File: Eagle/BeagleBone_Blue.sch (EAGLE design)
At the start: 153 parts, among them M1 JST_ZH_2, M2 JST_ZH_2, M3 JST_ZH_2, M4 JST_ZH_2, Q3 MOSFET-N, U1 OSD3358, U2 CM200C-32.768KAZF-UT, U3 DMC564040R, U4 DMC564040R, U5 24LC_32AT-I/OT

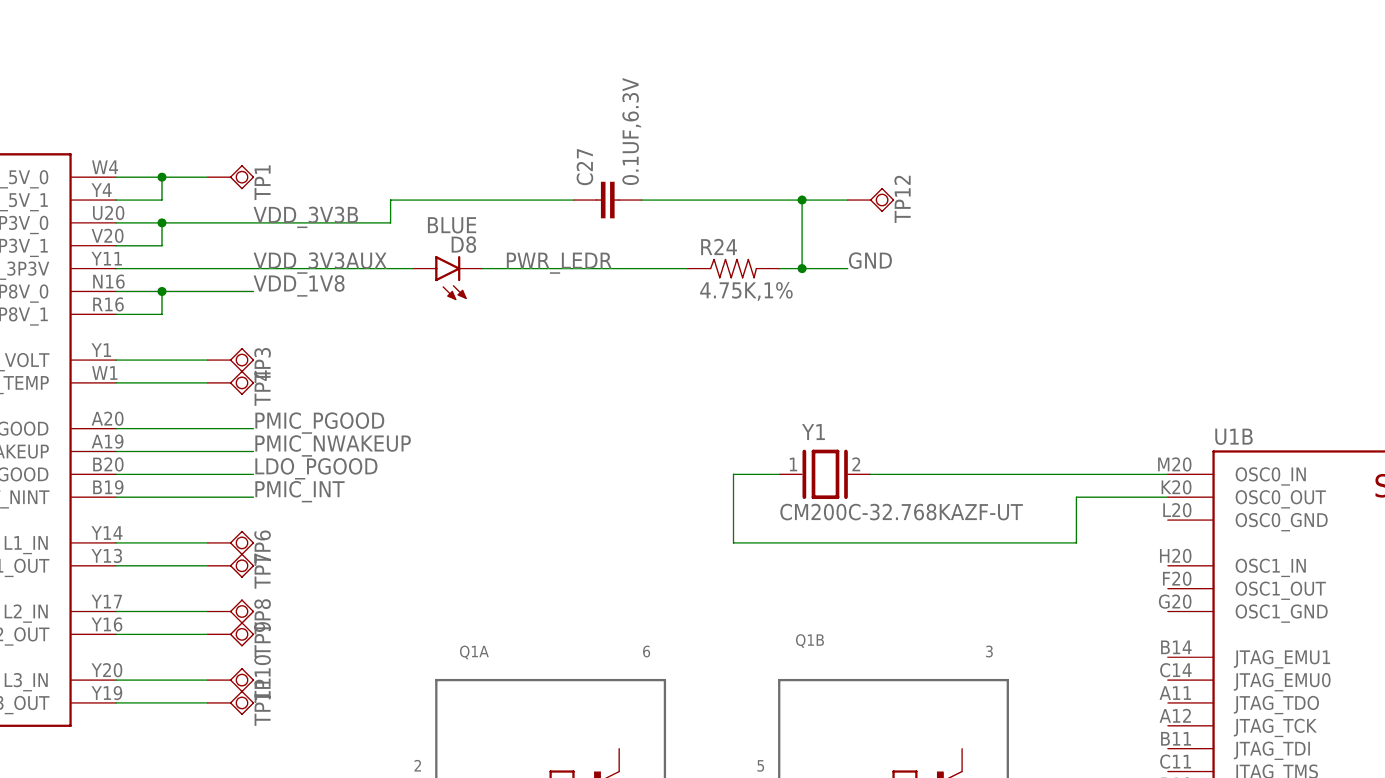
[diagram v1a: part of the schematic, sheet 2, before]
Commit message: Added crystals
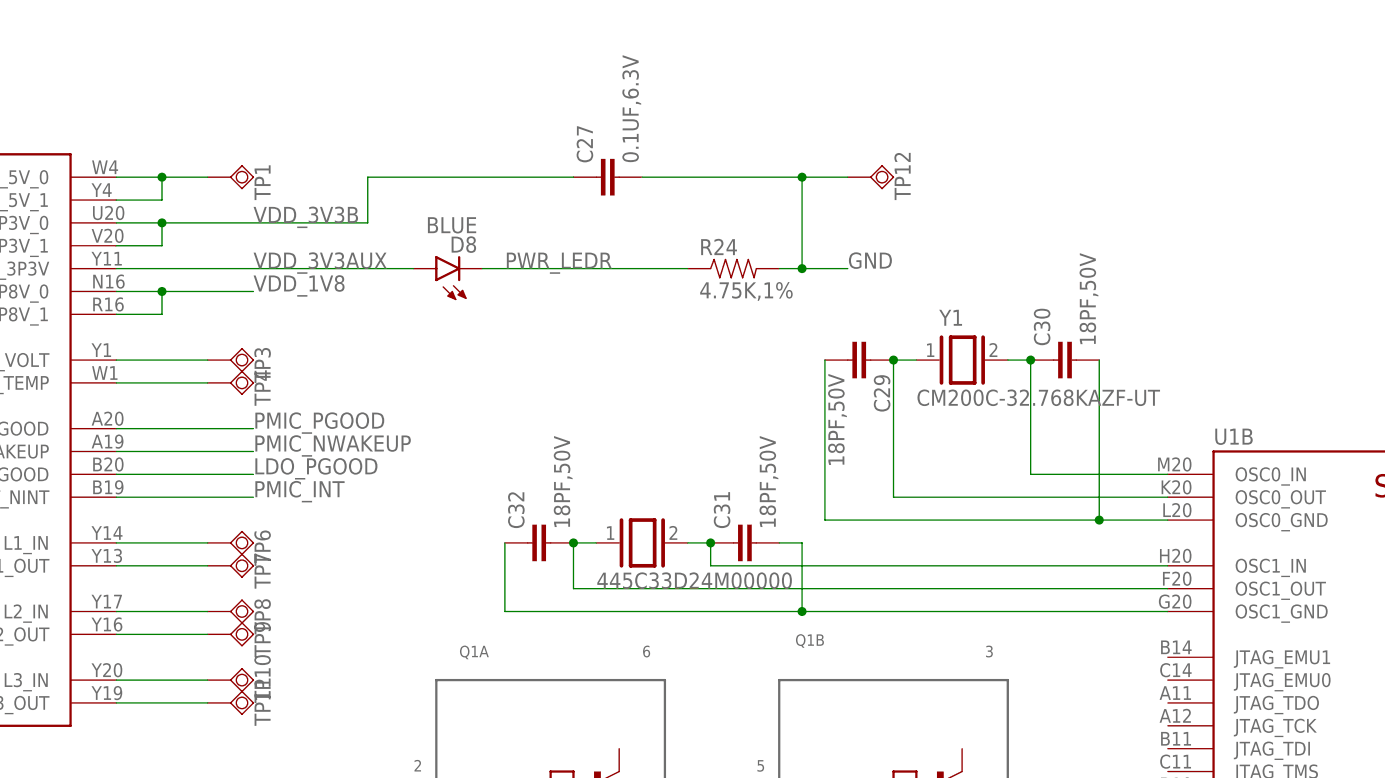
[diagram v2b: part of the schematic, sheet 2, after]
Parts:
- added C29, C30, C31, C32: 18PF,50V, Strawson_Eagle_Lib:CAP0402-CAP
- added Y2: 445C33D24M00000, 445C33D24M00000:445C33D24M00000
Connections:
- new net N$31: C29.2, C30.2, U1B.OSC0_GND
- new net N$32: C31.1, U1B.OSC1_IN, Y2.2
- new net N$33: C32.2, U1B.OSC1_OUT, Y2.1
- new net N$34: C31.2, C32.1, U1B.OSC1_GND
- net N$26: now also C30.1
- net N$27: now also C29.1
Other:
- moved on the sheet: C27, TP12
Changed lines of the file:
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@@
 <part name="TP13" library="testpad" deviceset="TPSQ" device="B1,27"/>
 <part name="C28" library="Strawson_Eagle_Lib" deviceset="CAP" device="0402-CAP" value="0.1UF,6.3V"/>
+<part name="C29" library="Strawson_Eagle_Lib" deviceset="CAP" device="0402-CAP" value="18PF,50V"/>
+<part name="C30" library="Strawson_Eagle_Lib" deviceset="CAP" device="0402-CAP" value="18PF,50V"/>
+<part name="Y2" library="445C33D24M00000" deviceset="445C33D24M00000" device=""/>
+<part name="C31" library="Strawson_Eagle_Lib" deviceset="CAP" device="0402-CAP" value="18PF,50V"/>
+<part name="C32" library="Strawson_Eagle_Lib" deviceset="CAP" device="0402-CAP" value="18PF,50V"/>
 </parts>
 <sheets>
@@
 <instance part="TP10" gate="G$1" x="137.16" y="193.04" rot="R90"/>
 <instance part="TP11" gate="G$1" x="137.16" y="190.5" rot="R90"/>
-<instance part="TP12" gate="G$1" x="208.28" y="246.38" rot="R90"/>
-<instance part="C27" gate="G$1" x="180.34" y="246.38" rot="R90"/>
-<instance part="U2" gate="G$1" x="251.46" y="203.2"/>
+<instance part="TP12" gate="G$1" x="208.28" y="248.92" rot="R90"/>
+<instance part="C27" gate="G$1" x="180.34" y="248.92" rot="R90"/>
+<instance part="U2" gate="G$1" x="266.7" y="215.9"/>
 <instance part="U3" gate="G$1" x="195.58" y="175.26"/>
 <instance part="U4" gate="G$1" x="195.58" y="134.62"/>
@@
 <instance part="TP13" gate="G$1" x="48.26" y="157.48" rot="R270"/>
 <instance part="C28" gate="G$1" x="25.4" y="160.02"/>
+<instance part="C29" gate="G$1" x="205.74" y="228.6" rot="R270"/>
+<instance part="C30" gate="G$1" x="231.14" y="228.6" rot="R90"/>
+<instance part="Y2" gate="G$1" x="226.06" y="198.12"/>
+<instance part="C31" gate="G$1" x="195.58" y="208.28" rot="R90"/>
+<instance part="C32" gate="G$1" x="172.72" y="208.28" rot="R90"/>
 </instances>
 <busses>
@@
 <junction x="129.54" y="243.84"/>
 <label x="139.7" y="243.84" size="1.778" layer="95"/>
-<wire x1="129.54" y1="243.84" x2="154.94" y2="243.84" width="0.1524" layer="91"/>
-<wire x1="154.94" y1="243.84" x2="154.94" y2="246.38" width="0.1524" layer="91"/>
+<wire x1="129.54" y1="243.84" x2="152.4" y2="243.84" width="0.1524" layer="91"/>
+<wire x1="152.4" y1="243.84" x2="152.4" y2="248.92" width="0.1524" layer="91"/>
 <pinref part="C27" gate="G$1" pin="1"/>
-<wire x1="154.94" y1="246.38" x2="175.26" y2="246.38" width="0.1524" layer="91"/>
+<wire x1="152.4" y1="248.92" x2="175.26" y2="248.92" width="0.1524" layer="91"/>
 </segment>
 </net>
@@
 <pinref part="TP12" gate="G$1" pin="TP"/>
 <pinref part="C27" gate="G$1" pin="2"/>
-<wire x1="182.88" y1="246.38" x2="200.66" y2="246.38" width="0.1524" layer="91"/>
-<wire x1="200.66" y1="246.38" x2="205.74" y2="246.38" width="0.1524" layer="91"/>
+<wire x1="182.88" y1="248.92" x2="200.66" y2="248.92" width="0.1524" layer="91"/>
+<wire x1="200.66" y1="248.92" x2="205.74" y2="248.92" width="0.1524" layer="91"/>
 <wire x1="205.74" y1="238.76" x2="200.66" y2="238.76" width="0.1524" layer="91"/>
-<wire x1="200.66" y1="238.76" x2="200.66" y2="246.38" width="0.1524" layer="91"/>
-<junction x="200.66" y="246.38"/>
+<wire x1="200.66" y1="238.76" x2="200.66" y2="248.92" width="0.1524" layer="91"/>
+<junction x="200.66" y="248.92"/>
 <junction x="200.66" y="238.76"/>
 </segment>
@@
 <net name="N$26" class="0">
 <segment>
+<pinref part="U2" gate="G$1" pin="2"/>
+<pinref part="C30" gate="G$1" pin="1"/>
+<wire x1="226.06" y1="228.6" x2="223.52" y2="228.6" width="0.1524" layer="91"/>
+<wire x1="226.06" y1="228.6" x2="226.06" y2="215.9" width="0.1524" layer="91"/>
+<junction x="226.06" y="228.6"/>
 <pinref part="U1" gate="B" pin="OSC0_IN"/>
-<pinref part="U2" gate="G$1" pin="2"/>
-<wire x1="241.3" y1="215.9" x2="208.28" y2="215.9" width="0.1524" layer="91"/>
+<wire x1="226.06" y1="215.9" x2="241.3" y2="215.9" width="0.1524" layer="91"/>
 </segment>
 </net>
@@
 <segment>
 <pinref part="U1" gate="B" pin="OSC0_OUT"/>
-<wire x1="241.3" y1="213.36" x2="231.14" y2="213.36" width="0.1524" layer="91"/>
-<wire x1="231.14" y1="213.36" x2="231.14" y2="208.28" width="0.1524" layer="91"/>
-<wire x1="231.14" y1="208.28" x2="193.04" y2="208.28" width="0.1524" layer="91"/>
-<wire x1="193.04" y1="208.28" x2="193.04" y2="215.9" width="0.1524" layer="91"/>
+<wire x1="241.3" y1="213.36" x2="210.82" y2="213.36" width="0.1524" layer="91"/>
+<wire x1="210.82" y1="213.36" x2="210.82" y2="228.6" width="0.1524" layer="91"/>
 <pinref part="U2" gate="G$1" pin="1"/>
-<wire x1="193.04" y1="215.9" x2="198.12" y2="215.9" width="0.1524" layer="91"/>
+<wire x1="210.82" y1="228.6" x2="213.36" y2="228.6" width="0.1524" layer="91"/>
+<pinref part="C29" gate="G$1" pin="1"/>
+<junction x="210.82" y="228.6"/>
 </segment>
 </net>
@@
 </segment>
 </net>
+<net name="N$31" class="0">
+<segment>
+<pinref part="U1" gate="B" pin="OSC0_GND"/>
+<wire x1="241.3" y1="210.82" x2="233.68" y2="210.82" width="0.1524" layer="91"/>
+<pinref part="C29" gate="G$1" pin="2"/>
+<wire x1="233.68" y1="210.82" x2="203.2" y2="210.82" width="0.1524" layer="91"/>
+<wire x1="203.2" y1="210.82" x2="203.2" y2="228.6" width="0.1524" layer="91"/>
+<pinref part="C30" gate="G$1" pin="2"/>
+<wire x1="233.68" y1="228.6" x2="233.68" y2="210.82" width="0.1524" layer="91"/>
+<junction x="233.68" y="210.82"/>
+</segment>
+</net>
+<net name="N$32" class="0">
+<segment>
+<pinref part="U1" gate="B" pin="OSC1_IN"/>
+<pinref part="C31" gate="G$1" pin="1"/>
+<wire x1="241.3" y1="205.74" x2="190.5" y2="205.74" width="0.1524" layer="91"/>
+<wire x1="190.5" y1="205.74" x2="190.5" y2="208.28" width="0.1524" layer="91"/>
+<pinref part="Y2" gate="G$1" pin="2"/>
+<wire x1="190.5" y1="208.28" x2="187.96" y2="208.28" width="0.1524" layer="91"/>
+<junction x="190.5" y="208.28"/>
+</segment>
+</net>
+<net name="N$33" class="0">
+<segment>
+<pinref part="U1" gate="B" pin="OSC1_OUT"/>
+<pinref part="C32" gate="G$1" pin="2"/>
+<wire x1="241.3" y1="203.2" x2="175.26" y2="203.2" width="0.1524" layer="91"/>
+<wire x1="175.26" y1="203.2" x2="175.26" y2="208.28" width="0.1524" layer="91"/>
+<pinref part="Y2" gate="G$1" pin="1"/>
+<wire x1="175.26" y1="208.28" x2="177.8" y2="208.28" width="0.1524" layer="91"/>
+<junction x="175.26" y="208.28"/>
+</segment>
+</net>
+<net name="N$34" class="0">
+<segment>
+<pinref part="C32" gate="G$1" pin="1"/>
+<wire x1="167.64" y1="208.28" x2="167.64" y2="200.66" width="0.1524" layer="91"/>
+<pinref part="U1" gate="B" pin="OSC1_GND"/>
+<wire x1="167.64" y1="200.66" x2="200.66" y2="200.66" width="0.1524" layer="91"/>
+<pinref part="C31" gate="G$1" pin="2"/>
+<wire x1="200.66" y1="200.66" x2="241.3" y2="200.66" width="0.1524" layer="91"/>
+<wire x1="198.12" y1="208.28" x2="200.66" y2="208.28" width="0.1524" layer="91"/>
+<wire x1="200.66" y1="208.28" x2="200.66" y2="200.66" width="0.1524" layer="91"/>
+<junction x="200.66" y="200.66"/>
+</segment>
+</net>

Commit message: Some PMIC connections
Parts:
- added TP14, TP15, TP16, TP17, TP18, TP19, TP20: TPSQB1,27, testpad:TPSQB1,27
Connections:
- new net N$35: TP14.TP, U1B.JTAG_EMU1
- new net N$36: TP15.TP, U1B.JTAG_EMU0
- new net N$37: TP16.TP, U1B.JTAG_TDO
- new net N$39: TP17.TP, U1B.JTAG_TCK
- new net N$40: TP18.TP, U1B.JTAG_TDI
- new net N$41: TP19.TP, U1B.JTAG_TMS
- new net N$42: TP20.TP, U1B.JTAG_TRSTN
- net LDO_PGOOD: now also U1B.RTC_PWRONRSTN
- net PMIC_INT: now also U1B.EXTINTN
- net PMIC_NWAKEUP: now also U1B.EXT_WAKEUP
- net PMIC_PGOOD: now also U1B.PWRONRSTN
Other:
- moved on the sheet: C29, C30, C31, C32, U1B

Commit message: Shuffle
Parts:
- added R59: 4.7K,1%, Strawson_Eagle_Lib:RESISTOR0402-RES
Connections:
- net GND: now also R59.1
- net I2C0_SCL: now also U5.SCL
- net N$42: now also R59.2
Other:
- moved on the sheet: C28, TP13, U1C, U5
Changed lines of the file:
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@@
 <part name="TP19" library="testpad" deviceset="TPSQ" device="B1,27"/>
 <part name="TP20" library="testpad" deviceset="TPSQ" device="B1,27"/>
+<part name="R59" library="Strawson_Eagle_Lib" deviceset="RESISTOR" device="0402-RES" value="4.7K,1%"/>
 </parts>
 <sheets>
@@
 <instance part="U1" gate="B" x="287.02" y="45.72"/>
 <instance part="U1" gate="A" x="71.12" y="187.96"/>
-<instance part="U1" gate="C" x="71.12" y="17.78"/>
+<instance part="U1" gate="C" x="45.72" y="17.78"/>
 <instance part="TP1" gate="G$1" x="137.16" y="248.92" rot="R90"/>
 <instance part="TP2" gate="G$1" x="45.72" y="228.6" rot="R270"/>
@@
 <instance part="C27" gate="G$1" x="180.34" y="248.92" rot="R90"/>
 <instance part="U2" gate="G$1" x="307.34" y="182.88"/>
-<instance part="U3" gate="G$1" x="236.22" y="142.24"/>
-<instance part="U4" gate="G$1" x="236.22" y="101.6"/>
-<instance part="U5" gate="A" x="73.66" y="170.18"/>
+<instance part="U3" gate="G$1" x="238.76" y="121.92"/>
+<instance part="U4" gate="G$1" x="165.1" y="121.92"/>
+<instance part="U5" gate="A" x="63.5" y="170.18"/>
 <instance part="R58" gate="G$1" x="50.8" y="162.56" rot="R180"/>
-<instance part="TP13" gate="G$1" x="48.26" y="157.48" rot="R270"/>
-<instance part="C28" gate="G$1" x="25.4" y="160.02"/>
+<instance part="TP13" gate="G$1" x="40.64" y="160.02" rot="R270"/>
+<instance part="C28" gate="G$1" x="17.78" y="160.02"/>
 <instance part="C29" gate="G$1" x="246.38" y="195.58" rot="R270"/>
 <instance part="C30" gate="G$1" x="271.78" y="195.58" rot="R90"/>
@@
 <instance part="TP19" gate="G$1" x="274.32" y="149.86" rot="R270"/>
 <instance part="TP20" gate="G$1" x="274.32" y="147.32" rot="R270"/>
+<instance part="R59" gate="G$1" x="254" y="162.56"/>
 </instances>
 <busses>
@@
 <wire x1="60.96" y1="195.58" x2="60.96" y2="165.1" width="0.1524" layer="91"/>
 <junction x="60.96" y="195.58"/>
-<wire x1="60.96" y1="165.1" x2="73.66" y2="165.1" width="0.1524" layer="91"/>
+<wire x1="60.96" y1="165.1" x2="63.5" y2="165.1" width="0.1524" layer="91"/>
+<pinref part="U5" gate="A" pin="SCL"/>
 </segment>
 </net>
@@
 <wire x1="55.88" y1="193.04" x2="55.88" y2="180.34" width="0.1524" layer="91"/>
 <junction x="55.88" y="193.04"/>
-<wire x1="55.88" y1="180.34" x2="114.3" y2="180.34" width="0.1524" layer="91"/>
-<wire x1="114.3" y1="180.34" x2="114.3" y2="170.18" width="0.1524" layer="91"/>
-<wire x1="114.3" y1="170.18" x2="109.22" y2="170.18" width="0.1524" layer="91"/>
+<wire x1="55.88" y1="180.34" x2="101.6" y2="180.34" width="0.1524" layer="91"/>
+<wire x1="101.6" y1="180.34" x2="101.6" y2="170.18" width="0.1524" layer="91"/>
+<wire x1="101.6" y1="170.18" x2="99.06" y2="170.18" width="0.1524" layer="91"/>
 <pinref part="U5" gate="A" pin="SDA"/>
 </segment>
@@
 <wire x1="53.34" y1="210.82" x2="53.34" y2="170.18" width="0.1524" layer="91"/>
 <pinref part="U5" gate="A" pin="VCC"/>
-<wire x1="53.34" y1="170.18" x2="73.66" y2="170.18" width="0.1524" layer="91"/>
+<wire x1="53.34" y1="170.18" x2="63.5" y2="170.18" width="0.1524" layer="91"/>
 <wire x1="53.34" y1="170.18" x2="40.64" y2="170.18" width="0.1524" layer="91"/>
 <junction x="53.34" y="170.18"/>
@@
 <wire x1="40.64" y1="162.56" x2="45.72" y2="162.56" width="0.1524" layer="91"/>
 <pinref part="C28" gate="G$1" pin="1"/>
-<wire x1="40.64" y1="170.18" x2="25.4" y2="170.18" width="0.1524" layer="91"/>
-<wire x1="25.4" y1="170.18" x2="25.4" y2="165.1" width="0.1524" layer="91"/>
+<wire x1="40.64" y1="170.18" x2="17.78" y2="170.18" width="0.1524" layer="91"/>
+<wire x1="17.78" y1="170.18" x2="17.78" y2="165.1" width="0.1524" layer="91"/>
 <junction x="40.64" y="170.18"/>
 </segment>
@@
 <segment>
 <pinref part="U5" gate="A" pin="VSS"/>
-<wire x1="73.66" y1="157.48" x2="68.58" y2="157.48" width="0.1524" layer="91"/>
-<wire x1="68.58" y1="157.48" x2="68.58" y2="149.86" width="0.1524" layer="91"/>
-<wire x1="68.58" y1="149.86" x2="25.4" y2="149.86" width="0.1524" layer="91"/>
+<wire x1="63.5" y1="157.48" x2="60.96" y2="157.48" width="0.1524" layer="91"/>
+<wire x1="60.96" y1="157.48" x2="60.96" y2="149.86" width="0.1524" layer="91"/>
+<wire x1="60.96" y1="149.86" x2="17.78" y2="149.86" width="0.1524" layer="91"/>
 <pinref part="C28" gate="G$1" pin="2"/>
-<wire x1="25.4" y1="149.86" x2="25.4" y2="157.48" width="0.1524" layer="91"/>
-<label x="30.48" y="149.86" size="1.778" layer="95"/>
+<wire x1="17.78" y1="149.86" x2="17.78" y2="157.48" width="0.1524" layer="91"/>
+<label x="33.02" y="149.86" size="1.778" layer="95"/>
+</segment>
+<segment>
+<pinref part="R59" gate="G$1" pin="1"/>
+<wire x1="248.92" y1="162.56" x2="231.14" y2="162.56" width="0.1524" layer="91"/>
+<label x="231.14" y="162.56" size="1.778" layer="95"/>
 </segment>
 </net>
@@
 <wire x1="55.88" y1="162.56" x2="60.96" y2="162.56" width="0.1524" layer="91"/>
 <pinref part="TP13" gate="G$1" pin="TP"/>
-<wire x1="60.96" y1="162.56" x2="73.66" y2="162.56" width="0.1524" layer="91"/>
-<wire x1="50.8" y1="157.48" x2="60.96" y2="157.48" width="0.1524" layer="91"/>
-<wire x1="60.96" y1="157.48" x2="60.96" y2="162.56" width="0.1524" layer="91"/>
+<wire x1="60.96" y1="162.56" x2="63.5" y2="162.56" width="0.1524" layer="91"/>
+<wire x1="43.18" y1="160.02" x2="60.96" y2="160.02" width="0.1524" layer="91"/>
+<wire x1="60.96" y1="160.02" x2="60.96" y2="162.56" width="0.1524" layer="91"/>
 <junction x="60.96" y="162.56"/>
 </segment>
@@
 <segment>
 <pinref part="U1" gate="B" pin="JTAG_TRSTN"/>
-<wire x1="276.86" y1="147.32" x2="281.94" y2="147.32" width="0.1524" layer="91"/>
+<wire x1="276.86" y1="147.32" x2="279.4" y2="147.32" width="0.1524" layer="91"/>
 <pinref part="TP20" gate="G$1" pin="TP"/>
-</segment>
-</net>
+<pinref part="R59" gate="G$1" pin="2"/>
+<wire x1="279.4" y1="147.32" x2="281.94" y2="147.32" width="0.1524" layer="91"/>
+<wire x1="259.08" y1="162.56" x2="266.7" y2="162.56" width="0.1524" layer="91"/>
+<wire x1="266.7" y1="162.56" x2="266.7" y2="144.78" width="0.1524" layer="91"/>
+<wire x1="266.7" y1="144.78" x2="279.4" y2="144.78" width="0.1524" layer="91"/>
+<wire x1="279.4" y1="144.78" x2="279.4" y2="147.32" width="0.1524" layer="91"/>
+<junction x="279.4" y="147.32"/>
+</segment>
+</net>
